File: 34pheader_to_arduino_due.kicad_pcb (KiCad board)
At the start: 2 copper layers, 7 parts

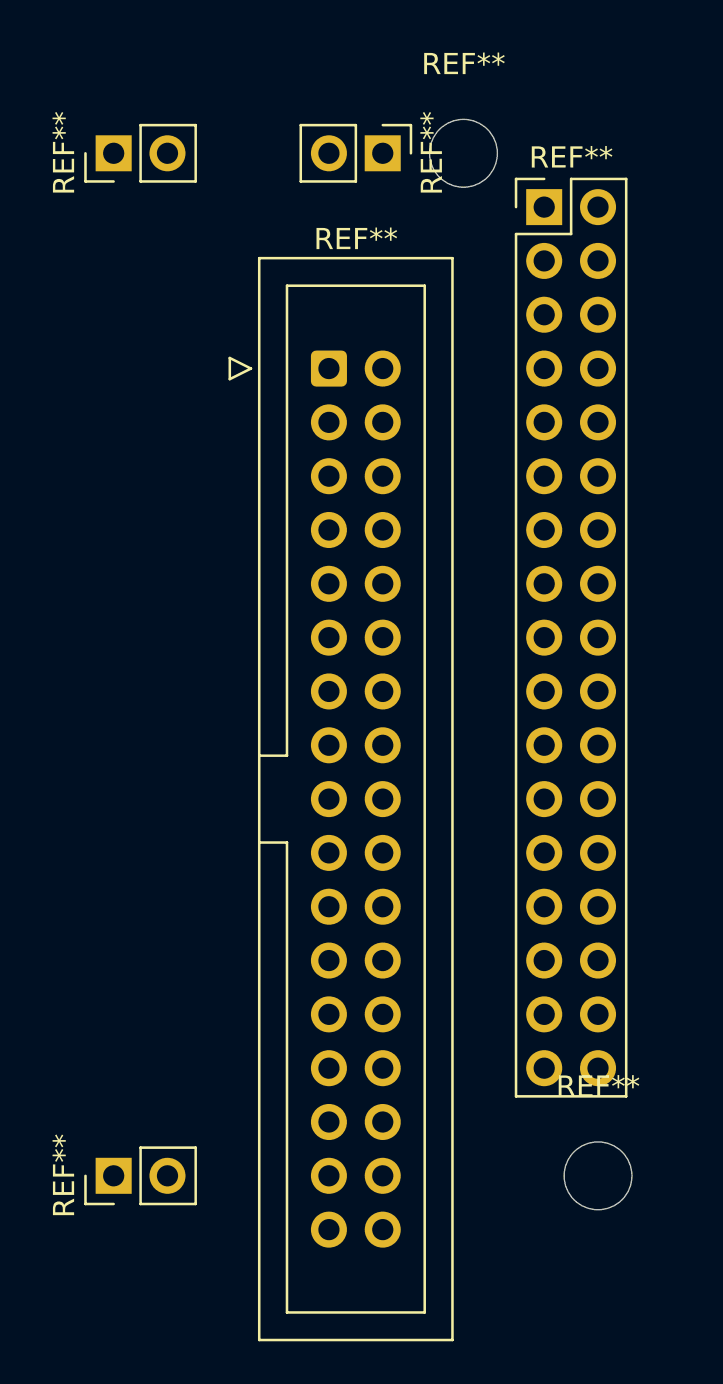
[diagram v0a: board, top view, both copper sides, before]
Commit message: Remove text labels, different header placement
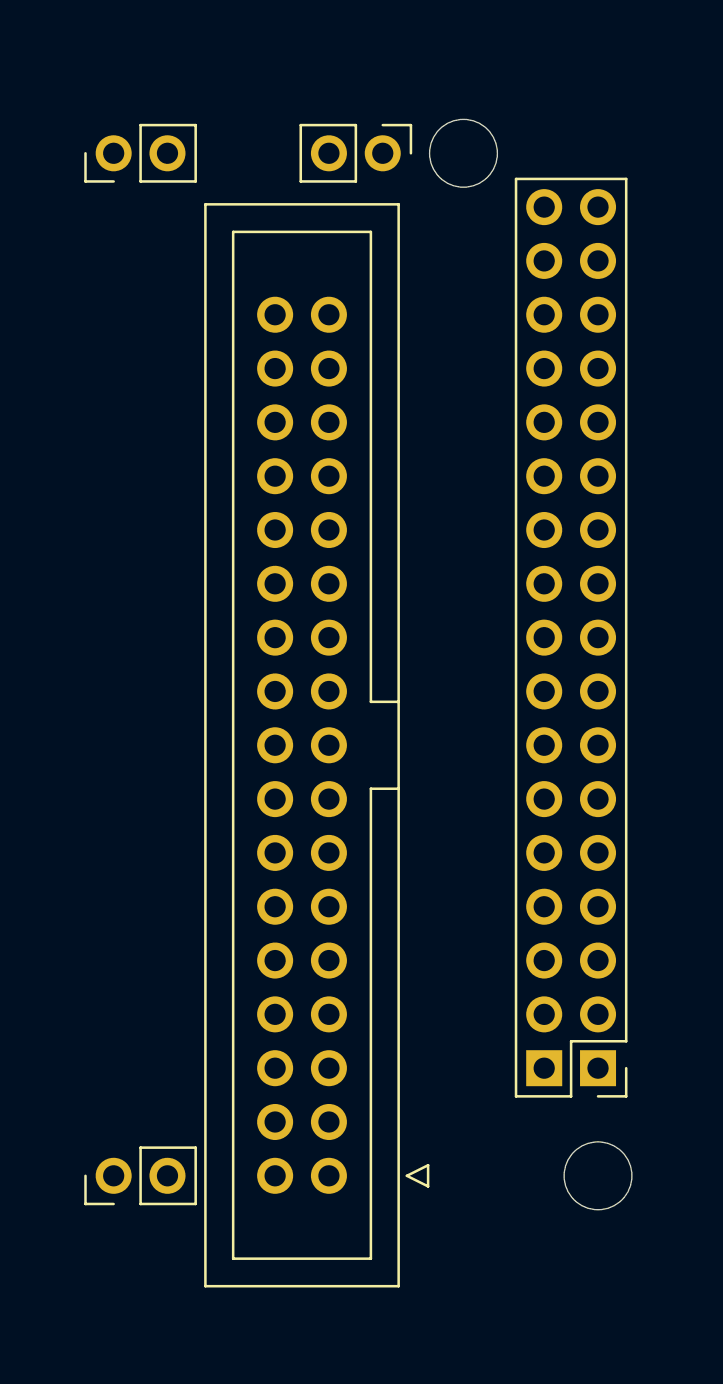
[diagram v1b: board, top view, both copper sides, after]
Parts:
- moved REF** 40.7 mm to (231.1, 66.0), turned to 180 degrees
- moved REF** 38.1 mm to (218.4, 71.1), turned to 180 degrees

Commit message: Move pin headers to back of the board
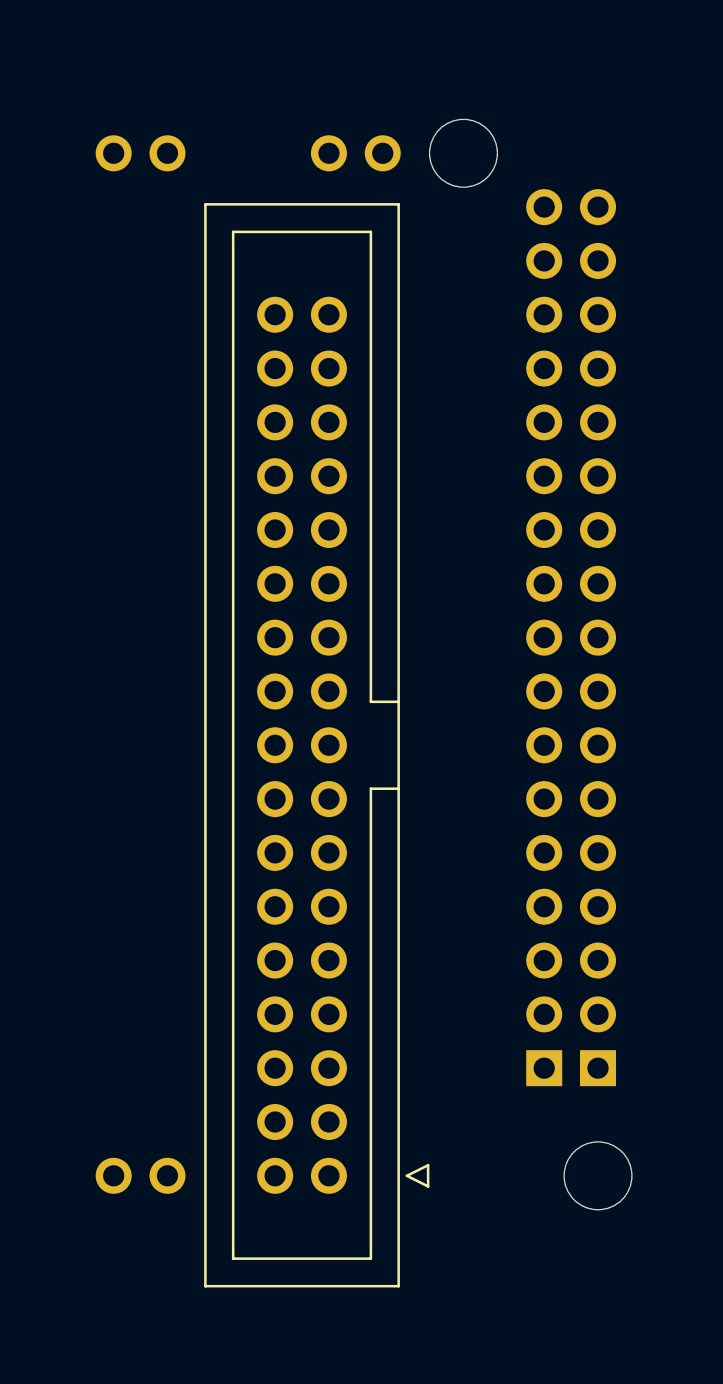
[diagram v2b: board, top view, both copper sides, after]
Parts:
- REF** (x4): moved to B.Cu
- moved REF** 2.54 mm to (210.8, 22.9)
- moved REF** 2.54 mm to (210.8, 71.1)
- moved REF** 2.54 mm to (218.4, 22.9)
- moved REF** 2.54 mm to (228.6, 66.0), turned to 0 degrees

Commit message: Add schema
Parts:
- J1: renamed from REF**; value IDC-Header_2x17_P2.54mm_Vertical -> Conn_02x17_Odd_Even
- J2: renamed from REF**; value PinHeader_2x17_P2.54mm_Vertical -> Conn_02x17_Odd_Even
- J3, J4, J5: renamed from REF**; value PinHeader_1x02_P2.54mm_Vertical -> Conn_01x02_Pin
- moved J3 2.54 mm to (221.0, 22.9), turned to 90 degrees
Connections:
- J1 pad 1: (no net) -> Net-(J1-Pin_1)
- J1 pad 10: (no net) -> Net-(J1-Pin_10)
- J1 pad 11: (no net) -> Net-(J1-Pin_11)
- J1 pad 12: (no net) -> Net-(J1-Pin_12)
- J1 pad 13: (no net) -> Net-(J1-Pin_13)
- J1 pad 14: (no net) -> Net-(J1-Pin_14)
- J1 pad 15: (no net) -> Net-(J1-Pin_15)
- J1 pad 16: (no net) -> Net-(J1-Pin_16)
- J1 pad 17: (no net) -> Net-(J1-Pin_17)
- J1 pad 18: (no net) -> Net-(J1-Pin_18)
- J1 pad 19: (no net) -> Net-(J1-Pin_19)
- J1 pad 2: (no net) -> Net-(J1-Pin_2)
- J1 pad 20: (no net) -> Net-(J1-Pin_20)
- J1 pad 21: (no net) -> Net-(J1-Pin_21)
- J1 pad 22: (no net) -> Net-(J1-Pin_22)
- J1 pad 23: (no net) -> Net-(J1-Pin_23)
- J1 pad 24: (no net) -> Net-(J1-Pin_24)
- J1 pad 25: (no net) -> Net-(J1-Pin_25)
- J1 pad 26: (no net) -> Net-(J1-Pin_26)
- J1 pad 27: (no net) -> Net-(J1-Pin_27)
- J1 pad 28: (no net) -> Net-(J1-Pin_28)
- J1 pad 29: (no net) -> Net-(J1-Pin_29)
- J1 pad 3: (no net) -> Net-(J1-Pin_3)
- J1 pad 30: (no net) -> Net-(J1-Pin_30)
- J1 pad 31: (no net) -> Net-(J1-Pin_31)
- J1 pad 32: (no net) -> Net-(J1-Pin_32)
- J1 pad 33: (no net) -> Net-(J1-Pin_33)
- J1 pad 34: (no net) -> Net-(J1-Pin_34)
- J1 pad 4: (no net) -> Net-(J1-Pin_4)
- J1 pad 5: (no net) -> Net-(J1-Pin_5)
- J1 pad 6: (no net) -> Net-(J1-Pin_6)
- J1 pad 7: (no net) -> Net-(J1-Pin_7)
- J1 pad 8: (no net) -> Net-(J1-Pin_8)
- J1 pad 9: (no net) -> Net-(J1-Pin_9)
- J2 pad 1: (no net) -> Net-(J1-Pin_16)
- J2 pad 10: (no net) -> Net-(J1-Pin_8)
- J2 pad 11: (no net) -> Net-(J1-Pin_9)
- J2 pad 12: (no net) -> Net-(J1-Pin_10)
- J2 pad 13: (no net) -> Net-(J1-Pin_11)
- J2 pad 14: (no net) -> Net-(J1-Pin_12)
- J2 pad 15: (no net) -> Net-(J1-Pin_13)
- J2 pad 16: (no net) -> unconnected-(J2-Pin_16-Pad16)
- J2 pad 17: (no net) -> Net-(J1-Pin_15)
- J2 pad 18: (no net) -> unconnected-(J2-Pin_18-Pad18)
- J2 pad 19: (no net) -> Net-(J1-Pin_17)
- J2 pad 2: (no net) -> Net-(J1-Pin_14)
- J2 pad 20: (no net) -> Net-(J1-Pin_18)
- J2 pad 21: (no net) -> Net-(J1-Pin_19)
- J2 pad 22: (no net) -> Net-(J1-Pin_20)
- J2 pad 23: (no net) -> Net-(J1-Pin_21)
- J2 pad 24: (no net) -> Net-(J1-Pin_22)
- J2 pad 25: (no net) -> Net-(J1-Pin_23)
- J2 pad 26: (no net) -> Net-(J1-Pin_24)
- J2 pad 27: (no net) -> Net-(J1-Pin_25)
- J2 pad 28: (no net) -> Net-(J1-Pin_26)
- J2 pad 29: (no net) -> Net-(J1-Pin_27)
- J2 pad 3: (no net) -> Net-(J1-Pin_1)
- J2 pad 30: (no net) -> Net-(J1-Pin_28)
- J2 pad 31: (no net) -> Net-(J1-Pin_29)
- J2 pad 32: (no net) -> Net-(J1-Pin_30)
- J2 pad 33: (no net) -> Net-(J1-Pin_31)
- J2 pad 34: (no net) -> Net-(J1-Pin_32)
- J2 pad 4: (no net) -> Net-(J1-Pin_2)
- J2 pad 5: (no net) -> Net-(J1-Pin_3)
- J2 pad 6: (no net) -> Net-(J1-Pin_4)
- J2 pad 7: (no net) -> Net-(J1-Pin_5)
- J2 pad 8: (no net) -> Net-(J1-Pin_6)
- J2 pad 9: (no net) -> Net-(J1-Pin_7)
- J3 pad 1: (no net) -> Net-(J1-Pin_33)
- J3 pad 2: (no net) -> Net-(J1-Pin_34)
- J4 pad 1: (no net) -> unconnected-(J4-Pin_1-Pad1)
- J4 pad 2: (no net) -> unconnected-(J4-Pin_2-Pad2)
- J5 pad 1: (no net) -> unconnected-(J5-Pin_1-Pad1)
- J5 pad 2: (no net) -> unconnected-(J5-Pin_2-Pad2)

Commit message: Continue on board design
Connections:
- J1 pad 16: Net-(J1-Pin_16) -> Net-(J1-Pin_14)
- J2 pad 1: Net-(J1-Pin_16) -> Net-(J1-Pin_14)
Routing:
- net Net-(J1-Pin_14): track 0.00 -> 42.8 mm
- net Net-(J1-Pin_6): track 0.00 -> 15.9 mm
- net Net-(J1-Pin_2): track 0.00 -> 15.9 mm
- net Net-(J1-Pin_13): track 0.00 -> 15.9 mm
- net Net-(J1-Pin_1): track 0.00 -> 15.9 mm
- net Net-(J1-Pin_5): track 0.00 -> 15.9 mm
- net Net-(J1-Pin_32): track 0.00 -> 15.9 mm
- net Net-(J1-Pin_31): track 0.00 -> 15.9 mm
- net Net-(J1-Pin_15): track 0.00 -> 15.9 mm
- net Net-(J1-Pin_12): track 0.00 -> 15.9 mm
- net Net-(J1-Pin_11): track 0.00 -> 15.9 mm
- net Net-(J1-Pin_30): track 0.00 -> 15.9 mm
- net Net-(J1-Pin_29): track 0.00 -> 15.9 mm
- net Net-(J1-Pin_28): track 0.00 -> 15.9 mm
- net Net-(J1-Pin_27): track 0.00 -> 15.9 mm
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
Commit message: Draw an edge cut
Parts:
- moved J3 2.54 mm to (218.4, 22.9)
- renumbered REF** to MountingHole1, REF** to MountingHole2
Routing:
- net Net-(J1-Pin_14): track 42.8 -> 45.4 mm
- net Net-(J1-Pin_34): track 8.67 -> 7.62 mm
- net Net-(J1-Pin_33): track 8.67 -> 7.62 mm
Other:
- board outline added: 29 x 58 mm
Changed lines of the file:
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@@
     (tags "mounting hole 3.2mm no annular m3")
     (attr exclude_from_pos_files exclude_from_bom)
-    (fp_text reference "REF**" (at 0 -4.2) (layer "F.SilkS") hide
+    (fp_text reference "MountingHole1" (at 0 -4.2) (layer "F.SilkS") hide
         (effects (font (size 1 1) (thickness 0.15)))
     )
@@
     (fp_circle (center 0 0) (end 3.45 0)
       (stroke (width 0.05) (type solid)) (fill none) (layer "F.CrtYd"))
-    (pad "" np_thru_hole circle (at 0 0) (size 3.2 3.2) (drill 3.2) (layers "*.Cu" "*.Mask"))
+    (pad "" np_thru_hole circle (at 0 0) (size 3.2 3.2) (drill 3.2) (layers "F&B.Cu" "*.Mask"))
   )
   (footprint "MountingHole:MountingHole_3.2mm_M3" (layer "F.Cu")
@@
     (tags "mounting hole 3.2mm no annular m3")
     (attr exclude_from_pos_files exclude_from_bom)
-    (fp_text reference "REF**" (at 0 -4.2) (layer "F.SilkS") hide
+    (fp_text reference "MountingHole2" (at 0 -4.2) (layer "F.SilkS") hide
         (effects (font (size 1 1) (thickness 0.15)))
     )
@@
   )
   (footprint "Connector_PinHeader_2.54mm:PinHeader_1x02_P2.54mm_Vertical" (layer "B.Cu")
-    (at 220.98 22.86 90)
+    (at 218.44 22.86 90)
     (descr "Through hole straight pin header, 1x02, 2.54mm pitch, single row")
     (tags "Through hole pin header THT 1x02 2.54mm single row")
@@
     )
   )
+  (gr_rect (start 206 19) (end 235 77)
+    (stroke (width 0.05) (type default)) (fill none) (layer "Edge.Cuts"))
   (segment (start 219.71 71.12) (end 226.06 64.77) (width 0.25) (layer "B.Cu") (net 1))
   (segment (start 229.87 64.77) (end 231.14 63.5) (width 0.25) (layer "B.Cu") (net 1))
@@
   (segment (start 215.9 33.02) (end 217.17 31.75) (width 0.25) (layer "F.Cu") (net 30))
   (segment (start 222.25 31.75) (end 228.6 25.4) (width 0.25) (layer "F.Cu") (net 30))
-  (segment (start 220.98 27.94) (end 218.44 30.48) (width 0.25) (layer "F.Cu") (net 31))
-  (segment (start 220.98 22.86) (end 220.98 27.94) (width 0.25) (layer "F.Cu") (net 31))
-  (segment (start 218.44 27.94) (end 215.9 30.48) (width 0.25) (layer "F.Cu") (net 32))
-  (segment (start 218.44 22.86) (end 218.44 27.94) (width 0.25) (layer "F.Cu") (net 32))
-  (segment (start 220.98 73.66) (end 213.36 73.66) (width 0.5) (layer "F.Cu") (net 39))
-  (segment (start 214.63 55.88) (end 215.9 55.88) (width 0.5) (layer "F.Cu") (net 39))
-  (segment (start 213.36 57.15) (end 214.63 55.88) (width 0.5) (layer "F.Cu") (net 39))
-  (segment (start 213.36 73.66) (end 213.36 55.88) (width 0.5) (layer "F.Cu") (net 39))
-  (segment (start 213.36 55.88) (end 215.9 53.34) (width 0.5) (layer "F.Cu") (net 39))
-  (segment (start 228.6 66.04) (end 220.98 73.66) (width 0.5) (layer "F.Cu") (net 39))
+  (segment (start 218.44 30.48) (end 218.44 22.86) (width 0.25) (layer "F.Cu") (net 31))
+  (segment (start 215.9 30.48) (end 215.9 22.86) (width 0.25) (layer "F.Cu") (net 32))
+  (segment (start 220.98 73.66) (end 213.36 73.66) (width 1) (layer "F.Cu") (net 39))
+  (segment (start 214.63 55.88) (end 215.9 55.88) (width 1) (layer "F.Cu") (net 39))
+  (segment (start 228.6 66.04) (end 231.14 66.04) (width 1) (layer "F.Cu") (net 39))
+  (segment (start 213.36 57.15) (end 214.63 55.88) (width 1) (layer "F.Cu") (net 39))
+  (segment (start 213.36 73.66) (end 213.36 55.88) (width 1) (layer "F.Cu") (net 39))
+  (segment (start 213.36 55.88) (end 215.9 53.34) (width 1) (layer "F.Cu") (net 39))
+  (segment (start 228.6 66.04) (end 220.98 73.66) (width 1) (layer "F.Cu") (net 39))
 )

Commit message: Move IPC header away from the mounting hole
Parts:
- moved J1 1.27 mm to (218.4, 72.4)
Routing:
- net Net-(J1-Pin_14): track 45.4 -> 103.6 mm
- net Net-(J1-Pin_34): track 7.62 -> 8.89 mm
- net Net-(J1-Pin_33): track 7.62 -> 8.89 mm
- net Net-(J1-Pin_24): track 15.9 -> 16.4 mm
- net Net-(J1-Pin_23): track 15.9 -> 16.4 mm
- net Net-(J1-Pin_22): track 15.9 -> 16.4 mm
- net Net-(J1-Pin_21): track 15.9 -> 16.4 mm
- net Net-(J1-Pin_20): track 15.9 -> 16.4 mm
- net Net-(J1-Pin_19): track 15.9 -> 16.4 mm
- net Net-(J1-Pin_18): track 15.9 -> 16.4 mm
- net Net-(J1-Pin_17): track 15.9 -> 16.4 mm
- net Net-(J1-Pin_29): track 15.9 -> 16.4 mm
- net Net-(J1-Pin_27): track 15.9 -> 16.4 mm
- net Net-(J1-Pin_9): track 15.9 -> 16.4 mm
- net Net-(J1-Pin_8): track 15.9 -> 16.4 mm
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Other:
- board size 29 x 58 mm -> 29 x 59 mm
